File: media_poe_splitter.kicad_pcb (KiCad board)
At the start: 4 copper layers, 70.7 x 66.5 mm, 79 parts, among them IC1 LAN7850-I_8JX, IC2 17791063215, IC3 93AA66C-I/SN, J1 Screw_Terminal_01x02, Q1 DMP3099L-7, X1 7499811120, X2 68710614522, Y1 830055299

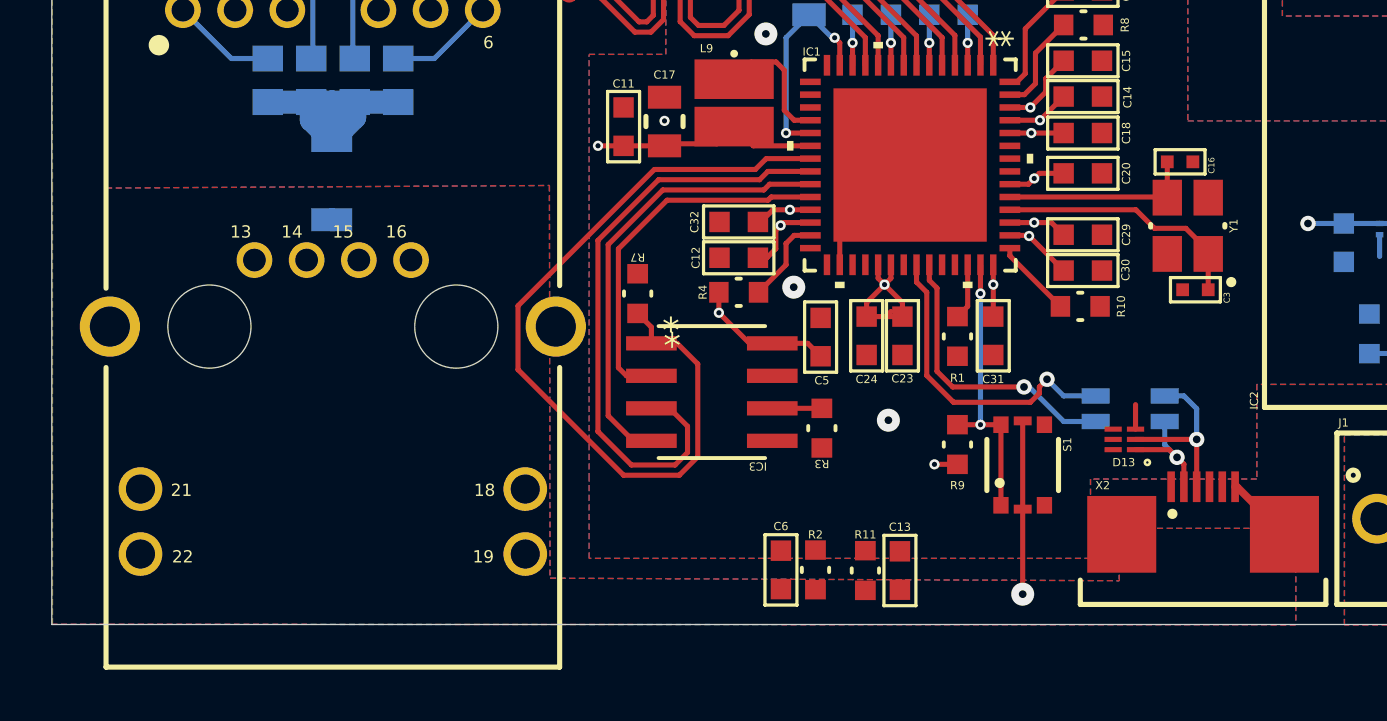
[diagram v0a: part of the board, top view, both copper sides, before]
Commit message: Add LEDs for Ethernet monitoring
Signed-off-by: Marc 'risson' Schmitt <marc.schmitt@risson.space>
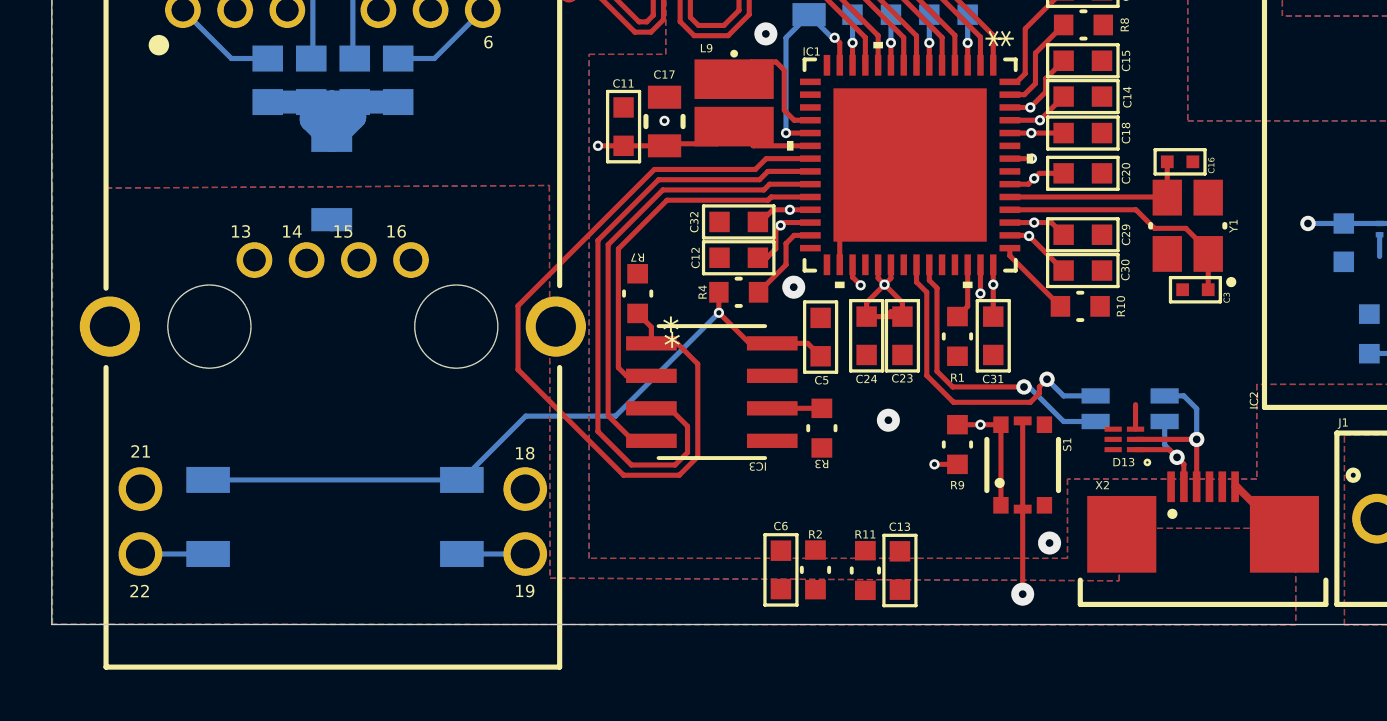
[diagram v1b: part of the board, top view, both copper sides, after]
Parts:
- added R12: 1K, RC1206FR-071KL:RC1206FR-071KL, B.Cu at (26.1, 82.3)
- added R13: 1K, RC1206FR-071KL:RC1206FR-071KL, B.Cu at (36.0, 82.3)
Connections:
- X1 pad 18: unconnected-(X1-LED2_G--Pad18) -> /LED2
- X1 pad 19: unconnected-(X1-LED2_G+-Pad19) -> Net-(X1-LED2_G+)
- X1 pad 21: unconnected-(X1-LED1_Y--Pad21) -> /LED0
- X1 pad 22: unconnected-(X1-LED1_Y+-Pad22) -> Net-(X1-LED1_Y+)
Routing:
- net /LED0: track 0.00 -> 32.4 mm, vias 0 -> 1
- net /LED2: track 0.00 -> 26.0 mm, vias 0 -> 1
- net +3V3: track 84.4 -> 108.0 mm
- net Net-(X1-LED1_Y+): track 0.00 -> 2.64 mm
- net Net-(X1-LED2_G+): track 0.00 -> 2.48 mm
- net GND: vias 6 -> 7

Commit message: Remove useless via
Signed-off-by: Marc 'risson' Schmitt <marc.schmitt@risson.space>
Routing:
- net GND: vias 7 -> 6
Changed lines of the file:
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@@
-	)
-	(via
-		(at 59 83.3)
-		(size 0.9)
-		(drill 0.3)
-		(layers "F.Cu" "B.Cu")
-		(free yes)
-		(net 34)
 	)
 	(via

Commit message: board, schematic: try to comply with ERC and DRC
Signed-off-by: Marc 'risson' Schmitt <marc.schmitt@risson.space>
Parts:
- moved C3 0.71 mm to (65.2, 73.9), turned to 90 degrees
- moved C16 0.71 mm to (63.6, 67.9), turned to -90 degrees

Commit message: Update vias, add logos
Signed-off-by: Marc 'risson' Schmitt <marc.schmitt@risson.space>
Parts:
- added G***: LOGO, logos:risson, B.Cu at (56.6, 55.1)
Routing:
- net GNDPWR: vias 67 -> 66
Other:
- board text added: "Apply thermal paste on thermal pads"
- board text added: "Thermal pad 1"
- board text added: "Thermal pad 2"
- board text added: "Thermal pad 3"
- board text added: "Thermal pad 4"
- board text added: "https://risson.space"

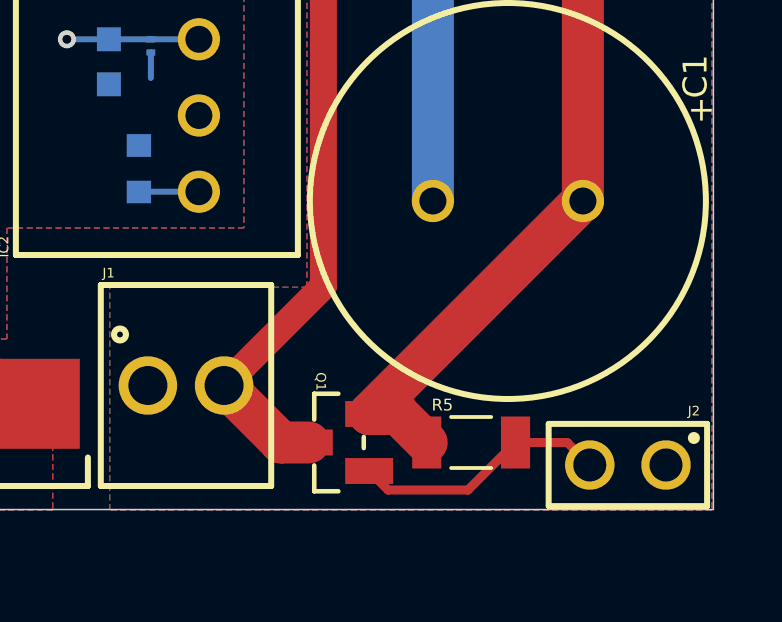
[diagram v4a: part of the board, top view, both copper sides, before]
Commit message: Update KiCad to 9.0
Signed-off-by: Marc 'risson' Schmitt <marc.schmitt@risson.space>
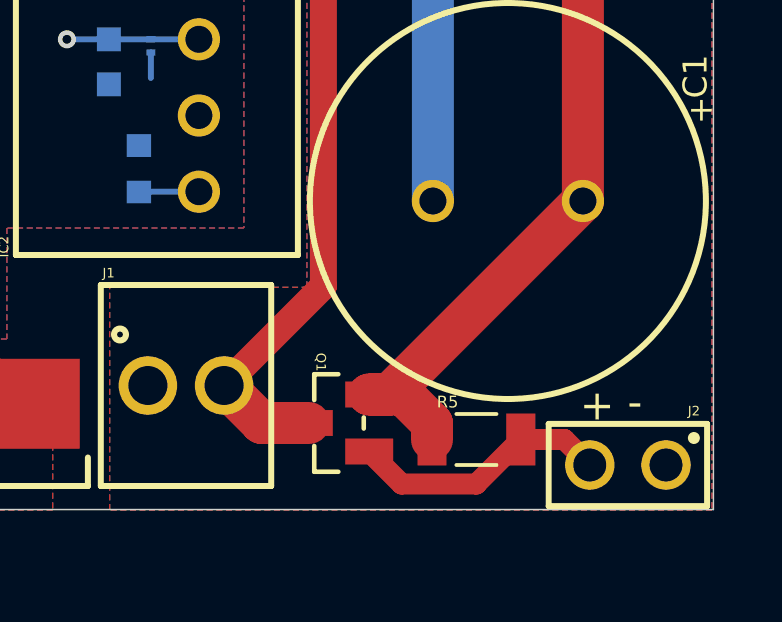
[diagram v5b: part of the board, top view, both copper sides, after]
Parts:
- moved Q1 0.65 mm to (78.2, 83.6)
- moved R5 0.20 mm to (82.8, 84.2)
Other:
- board text added: "+ -"

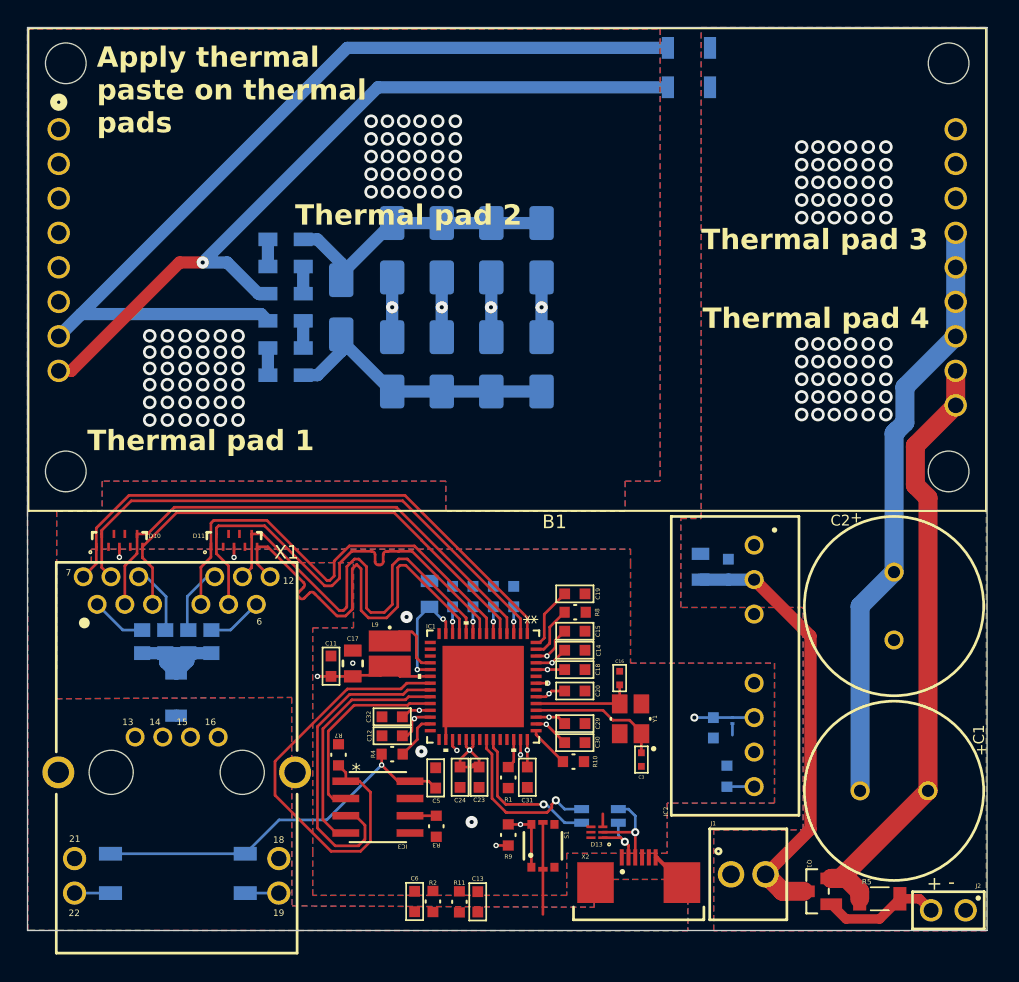
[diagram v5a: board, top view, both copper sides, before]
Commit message: Fix voltage issues, bigger traces where needed
Signed-off-by: Marc 'risson' Schmitt <marc.schmitt@risson.space>
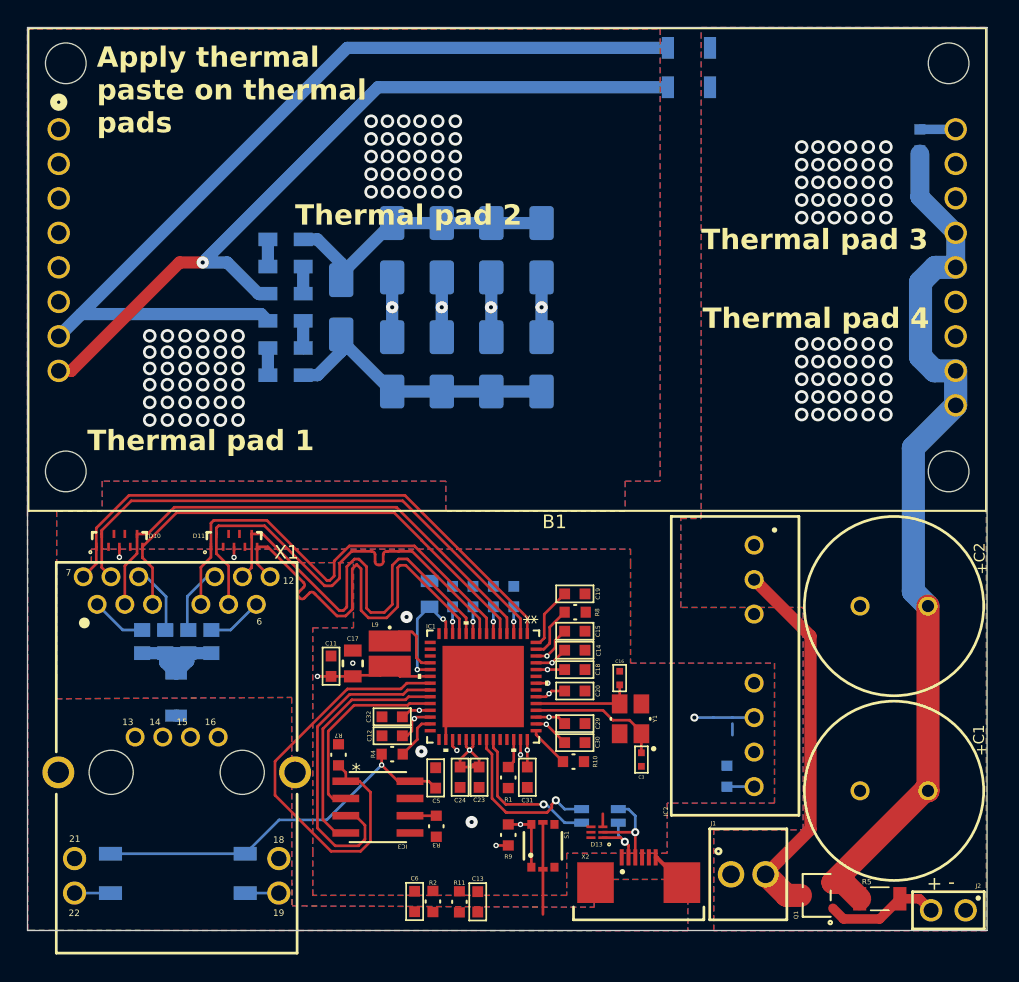
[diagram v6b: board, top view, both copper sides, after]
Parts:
- removed C10, C7: 100nF 25V, 885012206071:885012206071
- removed C4: 2.2uF 25V, 885012207079:885012207079
- removed C8: 10nF 6.3V, 885012104004:885012104004
- added R14: 8.2k, RC0603FR-078K2L:RC0603FR-078K2L, B.Cu at (85.7, 28.3)
- Q1: value DMP3099L-7 -> SSM3J358R,LF; footprint DMP3099L-7:DMP3099L-7 -> SSM3J358R,LF:SSM3J358R,LF
- R11, R2: value 330R -> 340R
- R6: value 47.8K -> 48.7K
- moved Q1 0.31 mm to (78.1, 83.9)
- turned C2 to 0 degrees
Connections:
- net +24V renamed +15V
- B1 pad 10: Net-(Q1-S) -> Net-(B1-VOUT1-Pad13)
- B1 pad 11: Net-(B1-0V2-Pad11) -> GNDA
- B1 pad 12: Net-(B1-0V2-Pad11) -> GNDA
- B1 pad 13: Net-(B1-0V2-Pad11) -> Net-(B1-VOUT1-Pad13)
- B1 pad 14: Net-(B1-0V2-Pad11) -> Net-(B1-VOUT1-Pad13)
- B1 pad 17: unconnected-(B1-ADJ-Pad17) -> Net-(B1-ADJ)
- B1 pad 9: Net-(Q1-S) -> Net-(B1-VOUT1-Pad13)
- C1 pad 1: Net-(Q1-S) -> Net-(B1-VOUT1-Pad13)
- C1 pad 2: Net-(B1-0V2-Pad11) -> GNDA
- C2 pad 1: Net-(B1-0V2-Pad11) -> Net-(B1-VOUT1-Pad13)
- Q1 pad 2: Net-(Q1-S) -> Net-(B1-VOUT1-Pad13)
- R5 pad 1: Net-(Q1-S) -> Net-(B1-VOUT1-Pad13)
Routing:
- net Net-(B1-VOUT1-Pad13): track 0.00 -> 65.9 mm
- net Net-(Q1-S): track 45.4 -> 0.00 mm
- net Net-(B1-0V2-Pad11): track 44.0 -> 0.00 mm
- net +15V: track 32.1 -> 28.0 mm
- net Net-(B1-ADJ): track 0.00 -> 2.64 mm
